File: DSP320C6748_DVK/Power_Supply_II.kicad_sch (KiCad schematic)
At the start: 39 parts, among them IC1 TPS650250RHBR

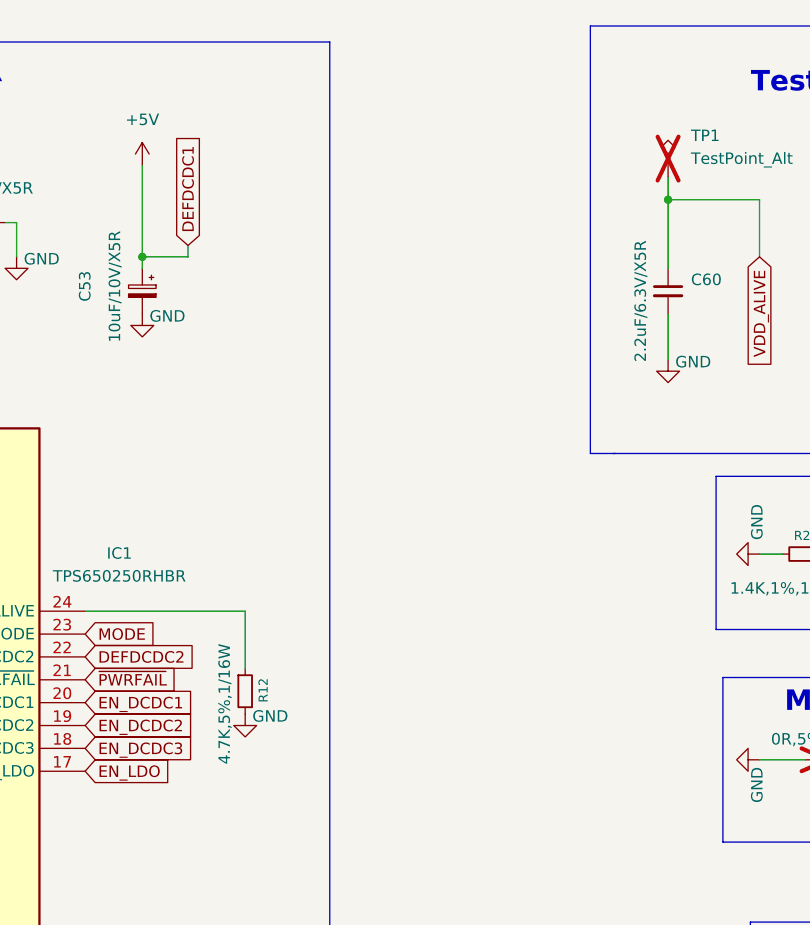
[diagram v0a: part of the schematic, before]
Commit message: NAND Flash circuit and Power Testpoints added
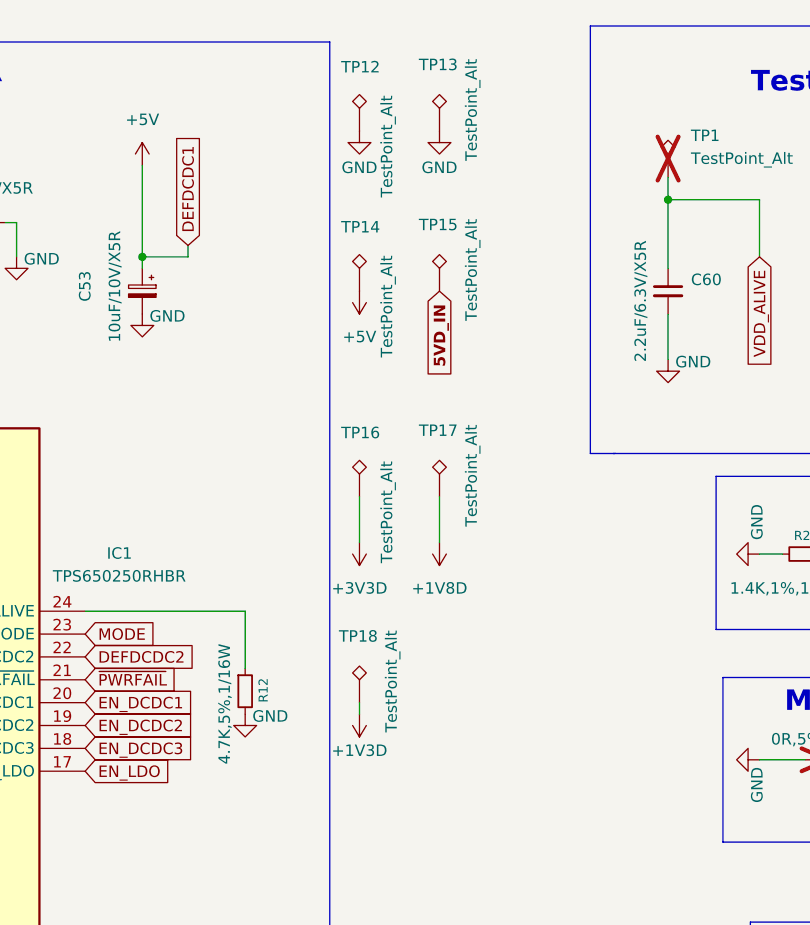
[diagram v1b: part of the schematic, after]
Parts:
- added TP12, TP13, TP14, TP15, TP16, TP17, TP18: TestPoint_Alt, symbol Connector:TestPoint_Alt
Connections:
- net +1V3D: now also TP18.1
- net +1V8D: now also TP17.1
- net +3V3D: now also TP16.1
- net +5V: now also TP14.1
- net GND: now also TP12.1, TP13.1
- new net 5VD_IN: TP15.1

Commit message: Whole Schematic Reannotation Done
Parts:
- renumbered C54 to C58, C58 to C59, C56 to C60, C55 to C61, C59 to C62, C57 to C63, C50 to C64, C61 to C65, C52 to C66, C64 to C67, C51 to C68, C65 to C69, C53 to C70, C60 to C71, IC1 to IC8, R24 to R54, R19 to R55, R8 to R56, R13 to R57, R26 to R58, R25 to R59, R18 to R60, R16 to R61, R17 to R62, R9 to R63, R12 to R64, R23 to R65, R15 to R66, R11 to R67, R10 to R68, R21 to R69, R22 to R70, R14 to R71, TP2 to TP10, TP12 to TP2, TP14 to TP3, TP16 to TP4, TP18 to TP5, TP13 to TP6, TP15 to TP7, TP17 to TP8, TP1 to TP9

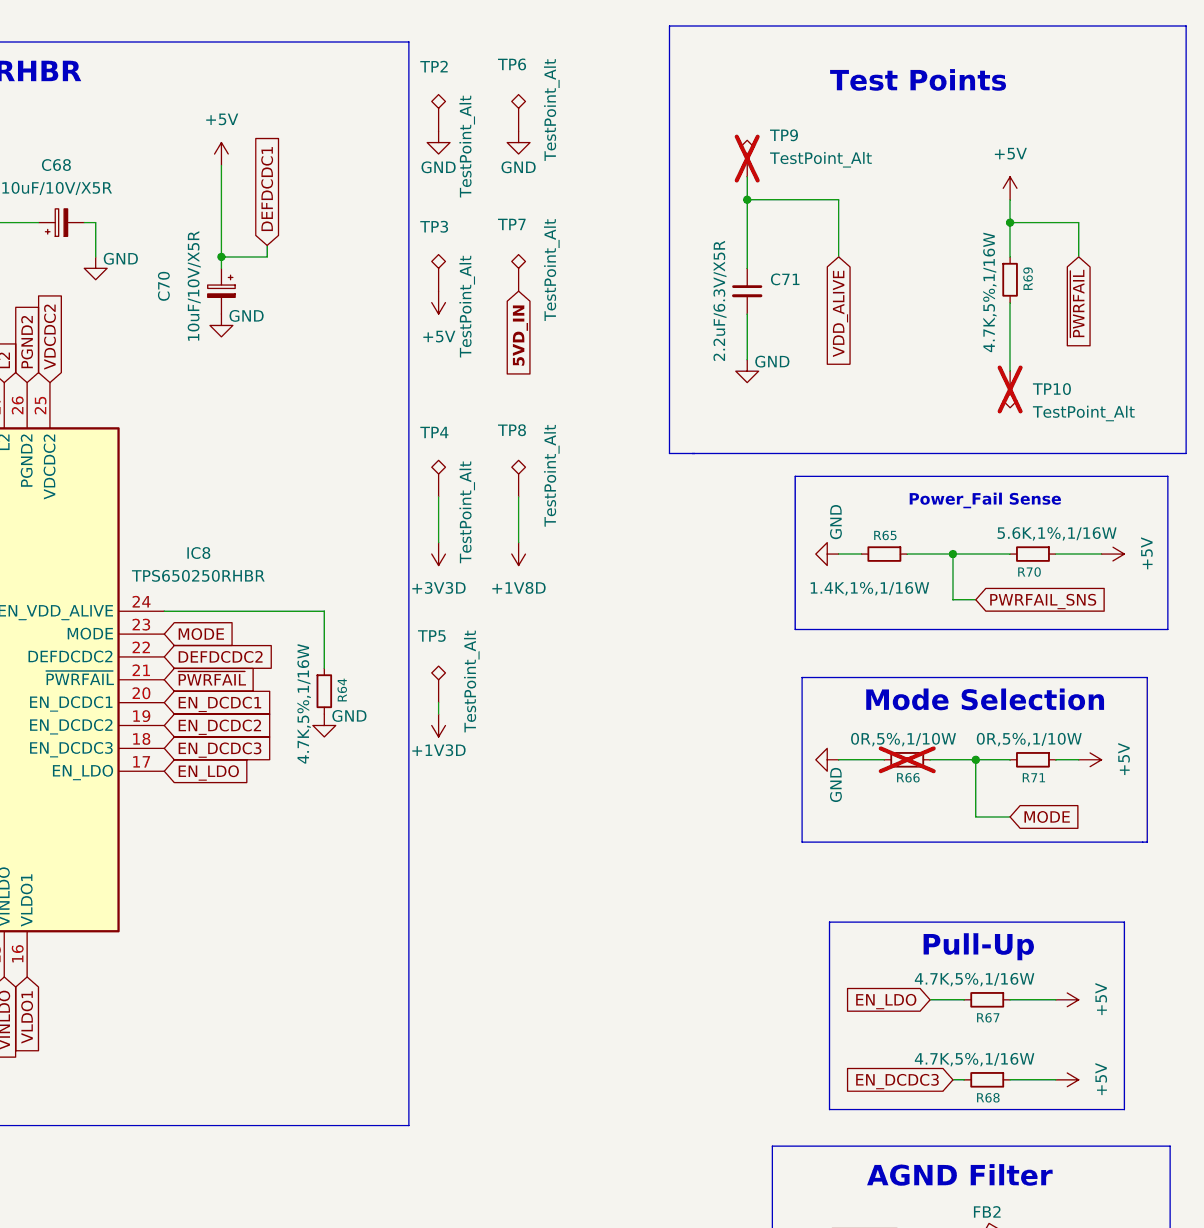
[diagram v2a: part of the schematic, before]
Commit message: Schematic corrections-I
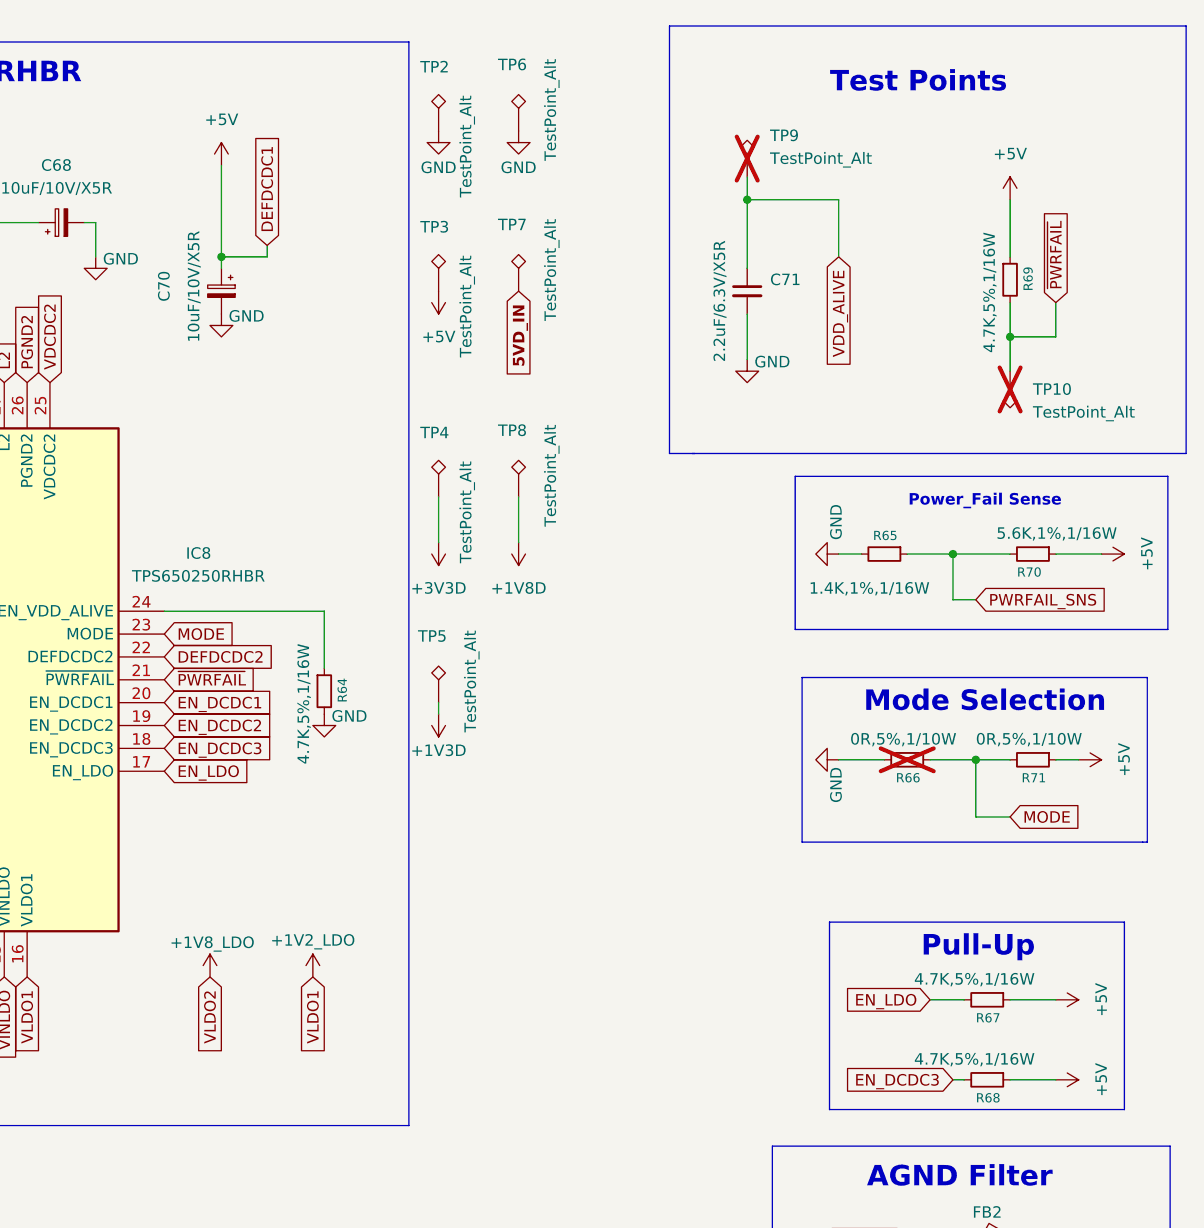
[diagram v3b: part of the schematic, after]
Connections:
- net +5V: no longer IC8.21 (~{PWRFAIL})
- net ~{PWRFAIL}: now reaches R69.2, TP10.1
- net ~{PWRFAIL}: now also IC8.21 (~{PWRFAIL})
- net VLDO1 renamed +1V2_LDO
- net VLDO2 renamed +1V8_LDO
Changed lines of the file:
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@@
 	)
 	(junction
+		(at 264.16 48.26)
+		(diameter 0)
+		(color 0 0 0 0)
+	)
+	(junction
 		(at 68.58 138.43)
 		(diameter 0)
@@
 	)
 	(junction
-		(at 264.16 35.56)
-		(diameter 0)
-		(color 0 0 0 0)
-	)
-	(junction
 		(at 80.01 185.42)
 		(diameter 0)
@@
 		)
 	)
-	(wire
-		(pts
-			(xy 271.78 39.37) (xy 271.78 35.56)
-		)
-		(stroke
-			(width 0)
-			(type default)
-		)
-	)
 	(polyline
 		(pts
@@
 	(wire
 		(pts
+			(xy 269.24 48.26) (xy 264.16 48.26)
+		)
+		(stroke
+			(width 0)
+			(type default)
+		)
+	)
+	(wire
+		(pts
 			(xy 252.73 148.59) (xy 259.08 148.59)
 		)
@@
 	(wire
 		(pts
-			(xy 264.16 44.45) (xy 264.16 52.07)
+			(xy 264.16 44.45) (xy 264.16 48.26)
 		)
 		(stroke
@@
 	(wire
 		(pts
-			(xy 271.78 35.56) (xy 264.16 35.56)
-		)
-		(stroke
-			(width 0)
-			(type default)
-		)
-	)
-	(wire
-		(pts
 			(xy 52.07 86.36) (xy 52.07 90.17)
 		)
@@
 	(wire
 		(pts
+			(xy 264.16 48.26) (xy 264.16 52.07)
+		)
+		(stroke
+			(width 0)
+			(type default)
+		)
+	)
+	(wire
+		(pts
 			(xy 234.95 33.02) (xy 234.95 40.64)
 		)
@@
 	(wire
 		(pts
+			(xy 269.24 44.45) (xy 269.24 48.26)
+		)
+		(stroke
+			(width 0)
+			(type default)
+		)
+	)
+	(wire
+		(pts
 			(xy 209.55 66.04) (xy 209.55 71.12)
 		)
@@
 	(wire
 		(pts
-			(xy 264.16 33.02) (xy 264.16 35.56)
+			(xy 264.16 33.02) (xy 264.16 39.37)
 		)
 		(stroke
@@
 		)
 	)
-	(wire
-		(pts
-			(xy 264.16 35.56) (xy 264.16 39.37)
-		)
-		(stroke
-			(width 0)
-			(type default)
-		)
-	)
 	(global_label "PM_1V2P"
 		(shape input)
@@
 		)
 	)
+	(global_label "VLDO2"
+		(shape input)
+		(at 175.26 119.38 270)
+		(effects
+			(font
+				(size 1.27 1.27)
+			)
+			(justify right)
+		)
+		(property "Intersheetrefs" "${INTERSHEET_REFS}"
+			(at 175.26 119.38 0)
+			(hide yes)
+			(show_name no)
+			(do_not_autoplace no)
+			(effects
+				(font
+					(size 1.27 1.27)
+				)
+			)
+		)
+	)
 	(global_label "DEFDCDC1"
 		(shape input)
@@
 		)
 	)
+	(global_label "VLDO1"
+		(shape input)
+		(at 186.69 119.38 270)
+		(effects
+			(font
+				(size 1.27 1.27)
+			)
+			(justify right)
+		)
+		(property "Intersheetrefs" "${INTERSHEET_REFS}"
+			(at 186.69 119.38 0)
+			(hide yes)
+			(show_name no)
+			(do_not_autoplace no)
+			(effects
+				(font
+					(size 1.27 1.27)
+				)
+			)
+		)
+	)
 	(global_label "L1"
 		(shape input)
@@
 	(global_label "~{PWRFAIL}"
 		(shape input)
-		(at 271.78 39.37 270)
+		(at 269.24 44.45 90)
 		(effects
 			(font
 				(size 1.27 1.27)
 			)
-			(justify right)
+			(justify left)
 		)
 		(property "Intersheetrefs" "${INTERSHEET_REFS}"
-			(at 271.78 39.37 90)
+			(at 269.24 44.45 90)
 			(hide yes)
 			(show_name no)
@@
 	)
 	(symbol
+		(lib_id "power:+1V2")
+		(at 186.69 119.38 0)
+		(unit 1)
+		(body_style 1)
+		(exclude_from_sim no)
+		(in_bom yes)
+		(on_board yes)
+		(in_pos_files yes)
+		(dnp no)
+		(property "Reference" "#PWR0380"
+			(at 186.69 123.19 0)
+			(hide yes)
+			(show_name no)
+			(do_not_autoplace no)
+			(effects
+				(font
+					(size 1.27 1.27)
+				)
+			)
+		)
+		(property "Value" "+1V2_LDO"
+			(at 186.69 115.316 0)
+			(show_name no)
+			(do_not_autoplace no)
+			(effects
+				(font
+					(size 1.27 1.27)
+				)
+			)
+		)
+		(property "Footprint" ""
+			(at 186.69 119.38 0)
+			(hide yes)
+			(show_name no)
+			(do_not_autoplace no)
+			(effects
+				(font
+					(size 1.27 1.27)
+				)
+			)
+		)
+		(property "Datasheet" ""
+			(at 186.69 119.38 0)
+			(hide yes)
+			(show_name no)
+			(do_not_autoplace no)
+			(effects
+				(font
+					(size 1.27 1.27)
+				)
+			)
+		)
+		(property "Description" "Power symbol creates a global label with name \"+1V2\""
+			(at 186.69 119.38 0)
+			(hide yes)
+			(show_name no)
+			(do_not_autoplace no)
+			(effects
+				(font
+					(size 1.27 1.27)
+				)
+			)
+		)
+		(pin "1"
+		)
+		(instances
+			(project "DSP320C6748_DVK"
+				(path "/3a70ffc0-9fe7-4a5b-b3c2-23140355df82/f23cd408-3269-44aa-9012-a7dd1d352757"
+					(reference "#PWR0380")
+					(unit 1)
+				)
+			)
+		)
+	)
+	(symbol
 		(lib_id "power:+5V")
 		(at 269.24 121.92 270)
@@
 					(unit 1)
 				)
+			)
+		)
+	)
+	(symbol
+		(lib_id "power:+1V8")
+		(at 175.26 119.38 0)
+		(unit 1)
+		(body_style 1)
+		(exclude_from_sim no)
+		(in_bom yes)
+		(on_board yes)
+		(in_pos_files yes)
+		(dnp no)
+		(property "Reference" "#PWR0379"
+			(at 175.26 123.19 0)
+			(hide yes)
+			(show_name no)
+			(do_not_autoplace no)
+			(effects
+				(font
+					(size 1.27 1.27)
+				)
+			)
+		)
+		(property "Value" "+1V8_LDO"
+			(at 175.514 115.57 0)
+			(show_name no)
+			(do_not_autoplace no)
+			(effects
+				(font
+					(size 1.27 1.27)
+				)
+			)
+		)
+		(property "Footprint" ""
+			(at 175.26 119.38 0)
+			(hide yes)
+			(show_name no)
+			(do_not_autoplace no)
+			(effects
+				(font
+					(size 1.27 1.27)
+				)
+			)
+		)
+		(property "Datasheet" ""
+			(at 175.26 119.38 0)
+			(hide yes)
+			(show_name no)
+			(do_not_autoplace no)
+			(effects
+				(font
+					(size 1.27 1.27)
+				)
+			)
+		)
+		(property "Description" "Power symbol creates a global label with name \"+1V8\""
+			(at 175.26 119.38 0)
+			(hide yes)
+			(show_name no)
+			(do_not_autoplace no)
+			(effects
+				(font
+					(size 1.27 1.27)
+				)
+			)
+		)
+		(pin "1"
+		)
+		(instances
+			(project "DSP320C6748_DVK"
+				(path "/3a70ffc0-9fe7-4a5b-b3c2-23140355df82/f23cd408-3269-44aa-9012-a7dd1d352757"
+					(reference "#PWR0379")
+					(unit 1)
+				)

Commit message: Schematic Corrections-II Done
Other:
- note added: "Note: Connect the VDCDCx Signals near the load end."
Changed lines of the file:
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@@
+		)
+	)
+	(text "Note:\nConnect the VDCDCx\nSignals near\nthe load end."
+		(exclude_from_sim no)
+		(at 97.536 126.492 0)
+		(effects
+			(font
+				(size 2.27 2.27)
+			)
+			(justify left)
 		)
 	)

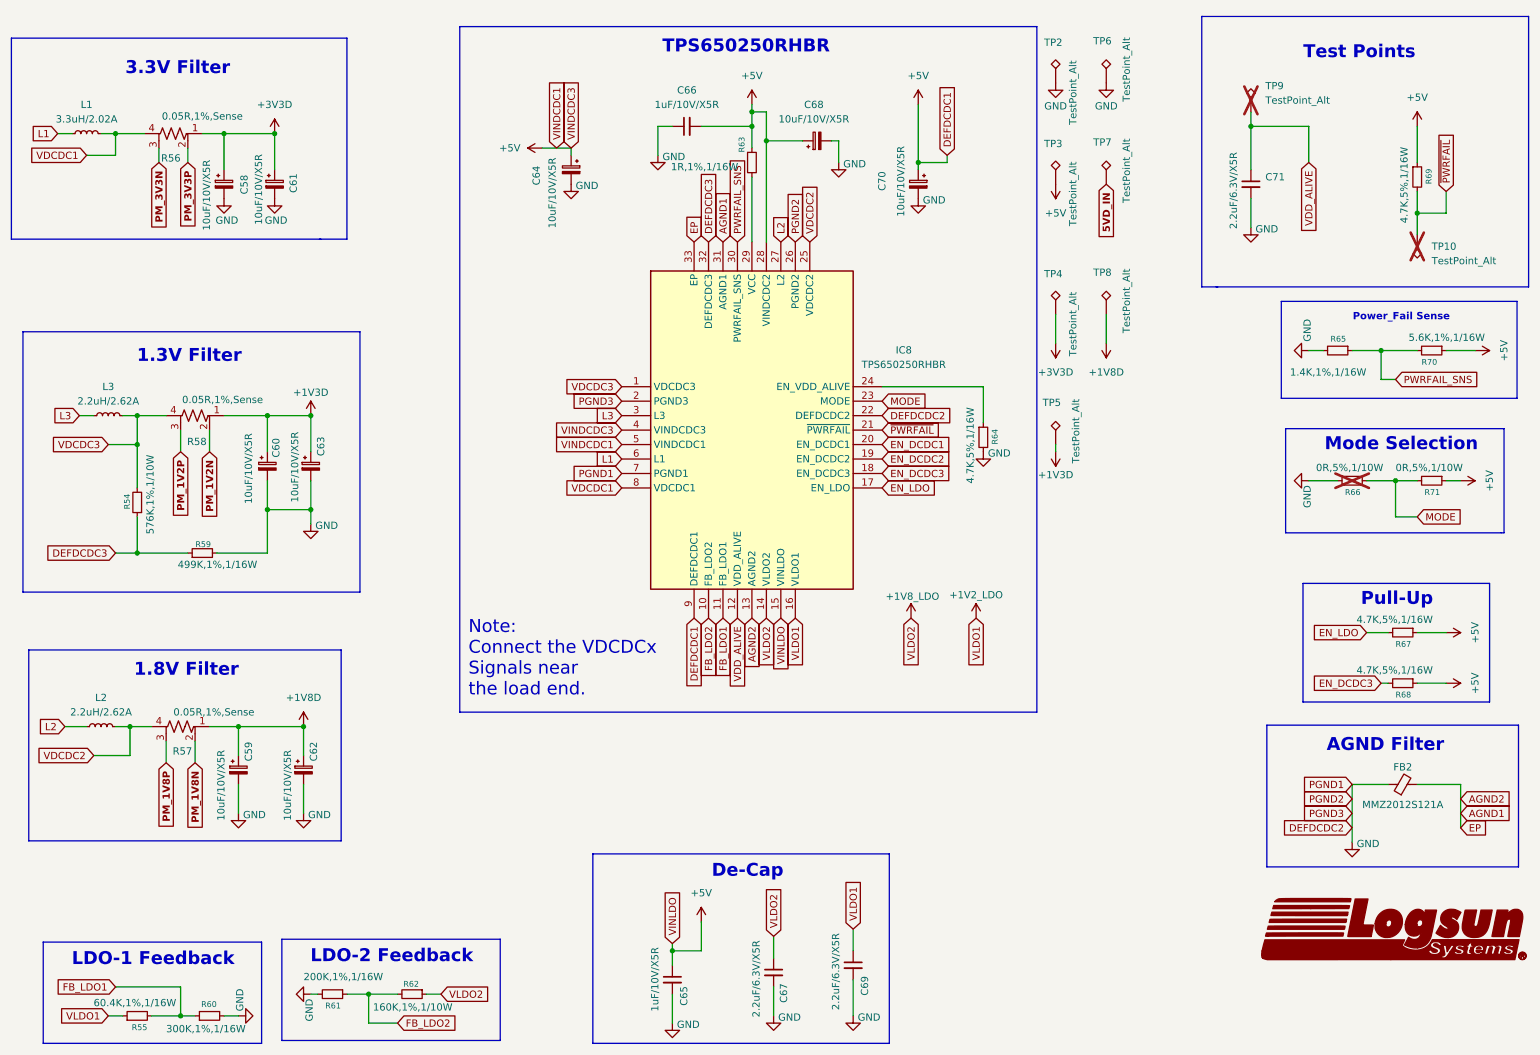
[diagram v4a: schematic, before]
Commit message: DC jack Replaced With Type-C, ADC and RTC section added
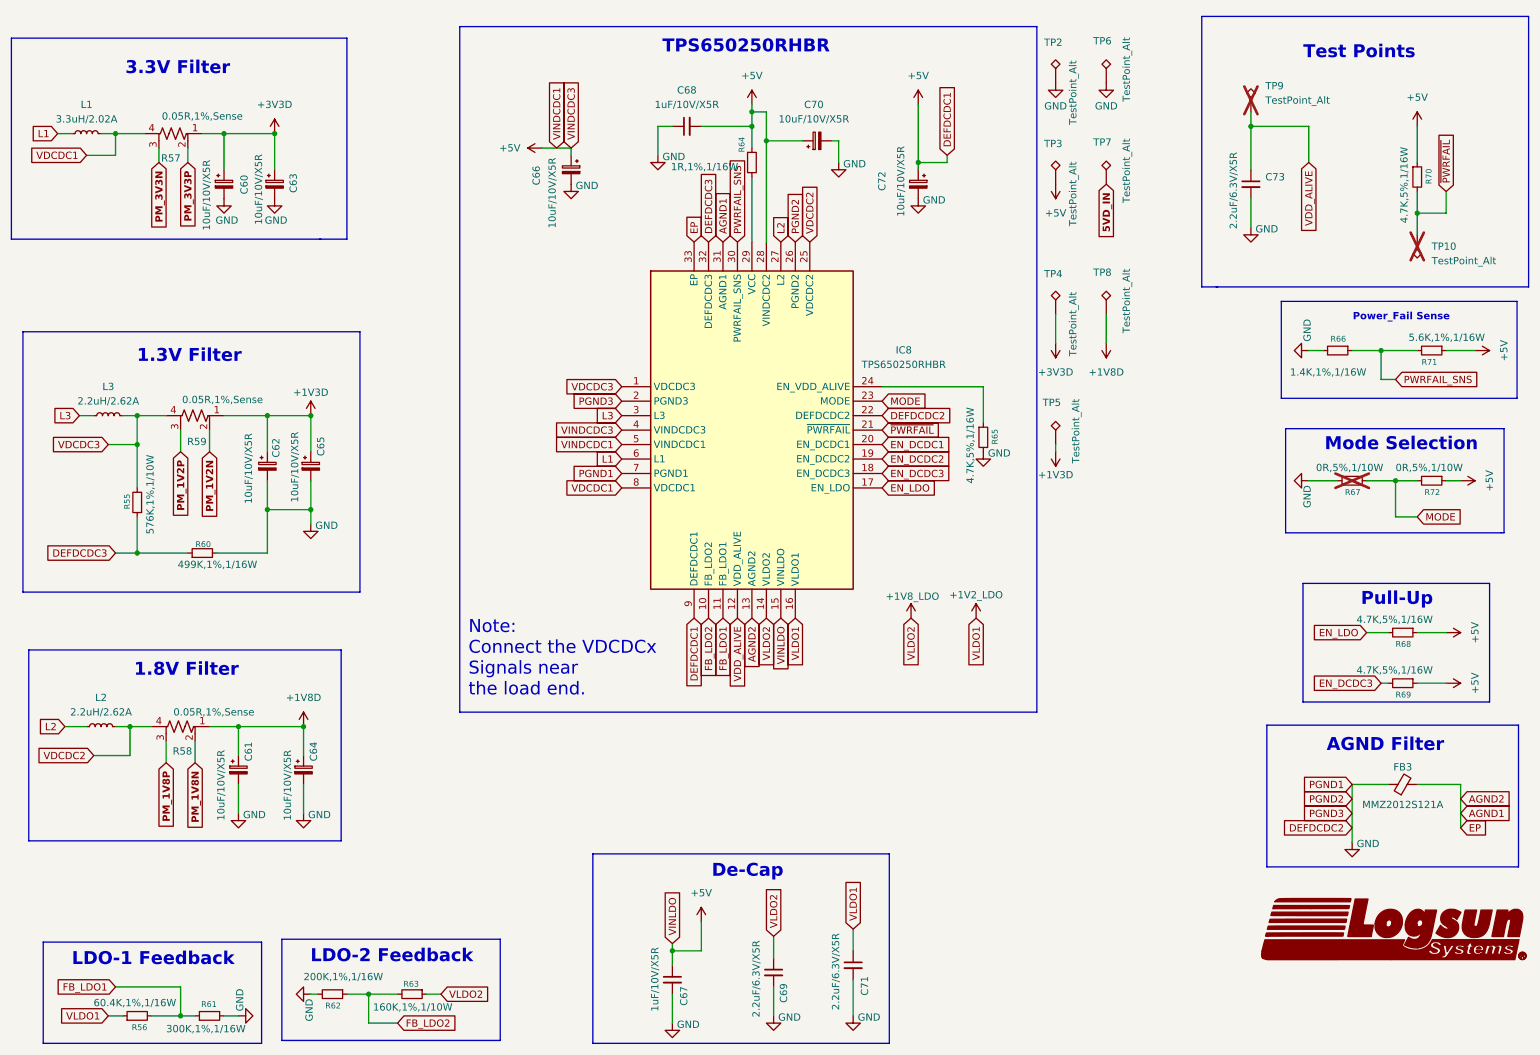
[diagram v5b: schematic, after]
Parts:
- renumbered C58 to C60, C59 to C61, C60 to C62, C61 to C63, C62 to C64, C63 to C65, C64 to C66, C65 to C67, C66 to C68, C67 to C69, C68 to C70, C69 to C71, C70 to C72, C71 to C73, FB2 to FB3, R54 to R55, R55 to R56, R56 to R57, R57 to R58, R58 to R59, R59 to R60, R60 to R61, R61 to R62, R62 to R63, R63 to R64, R64 to R65, R65 to R66, R66 to R67, R67 to R68, R68 to R69, R69 to R70, R70 to R71, R71 to R72
